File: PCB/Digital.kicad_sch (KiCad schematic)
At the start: 29 parts, among them IC1 MAX3051ESA+, J1 DE9_Pins_MountingHoles, J2 ICSP, J3 DE9_Plug_MountingHoles, J4 Conn_Coaxial, J6 Conn_01x03, J7 DOOR, J8 WINDOW, U1 PIC18F2580T-I/SO, Y2 ABLS

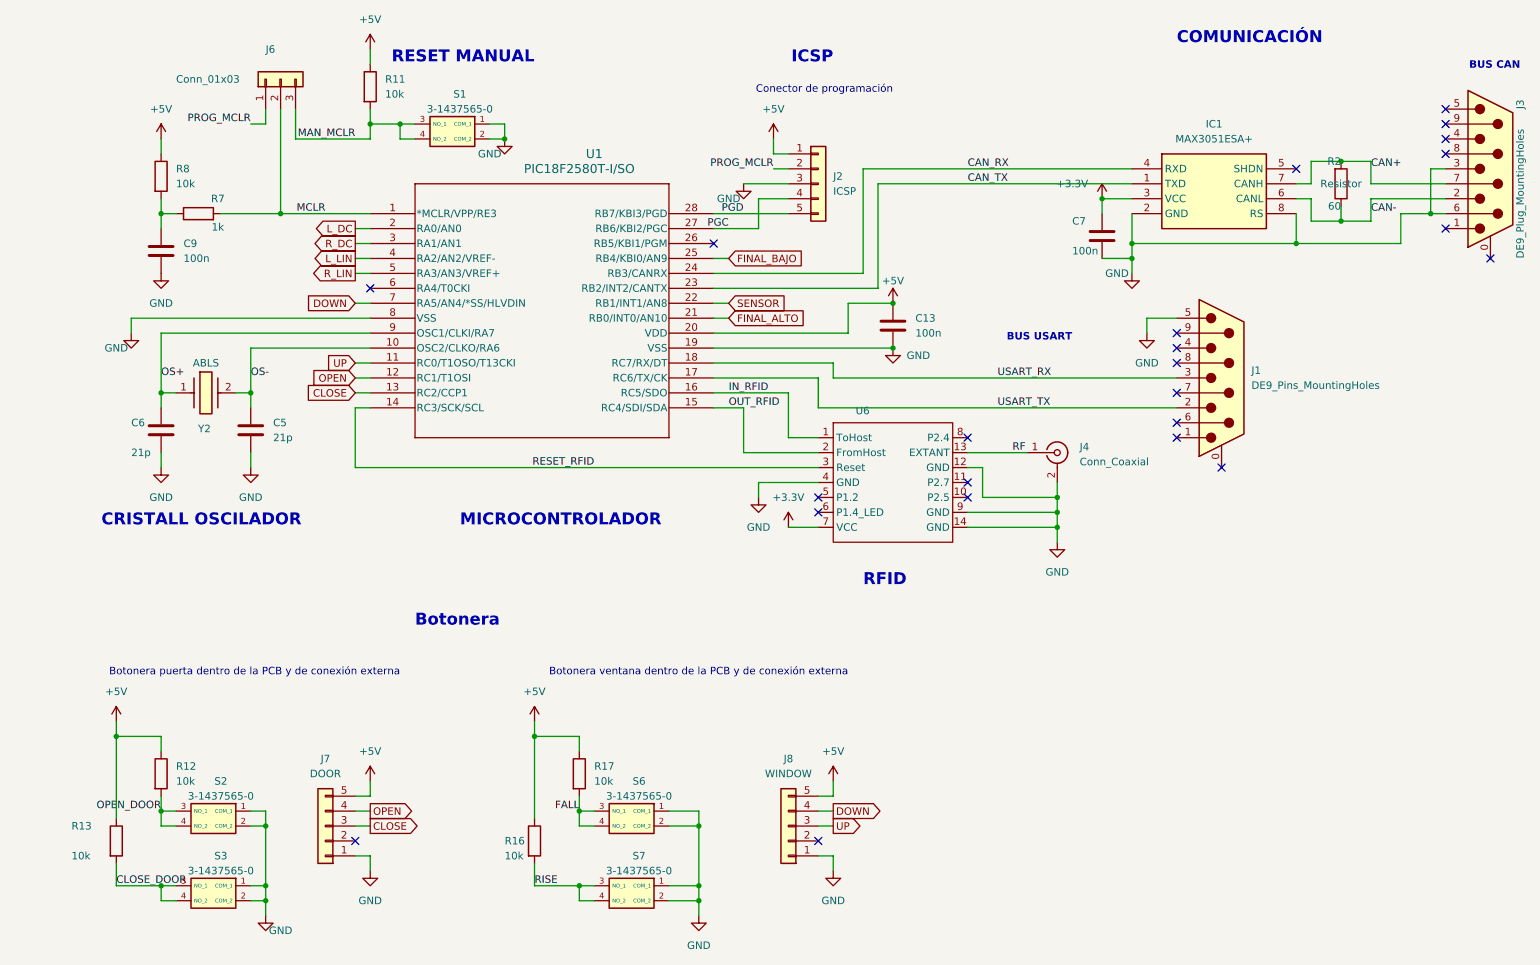
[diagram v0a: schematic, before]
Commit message: cambio de posición de los pines
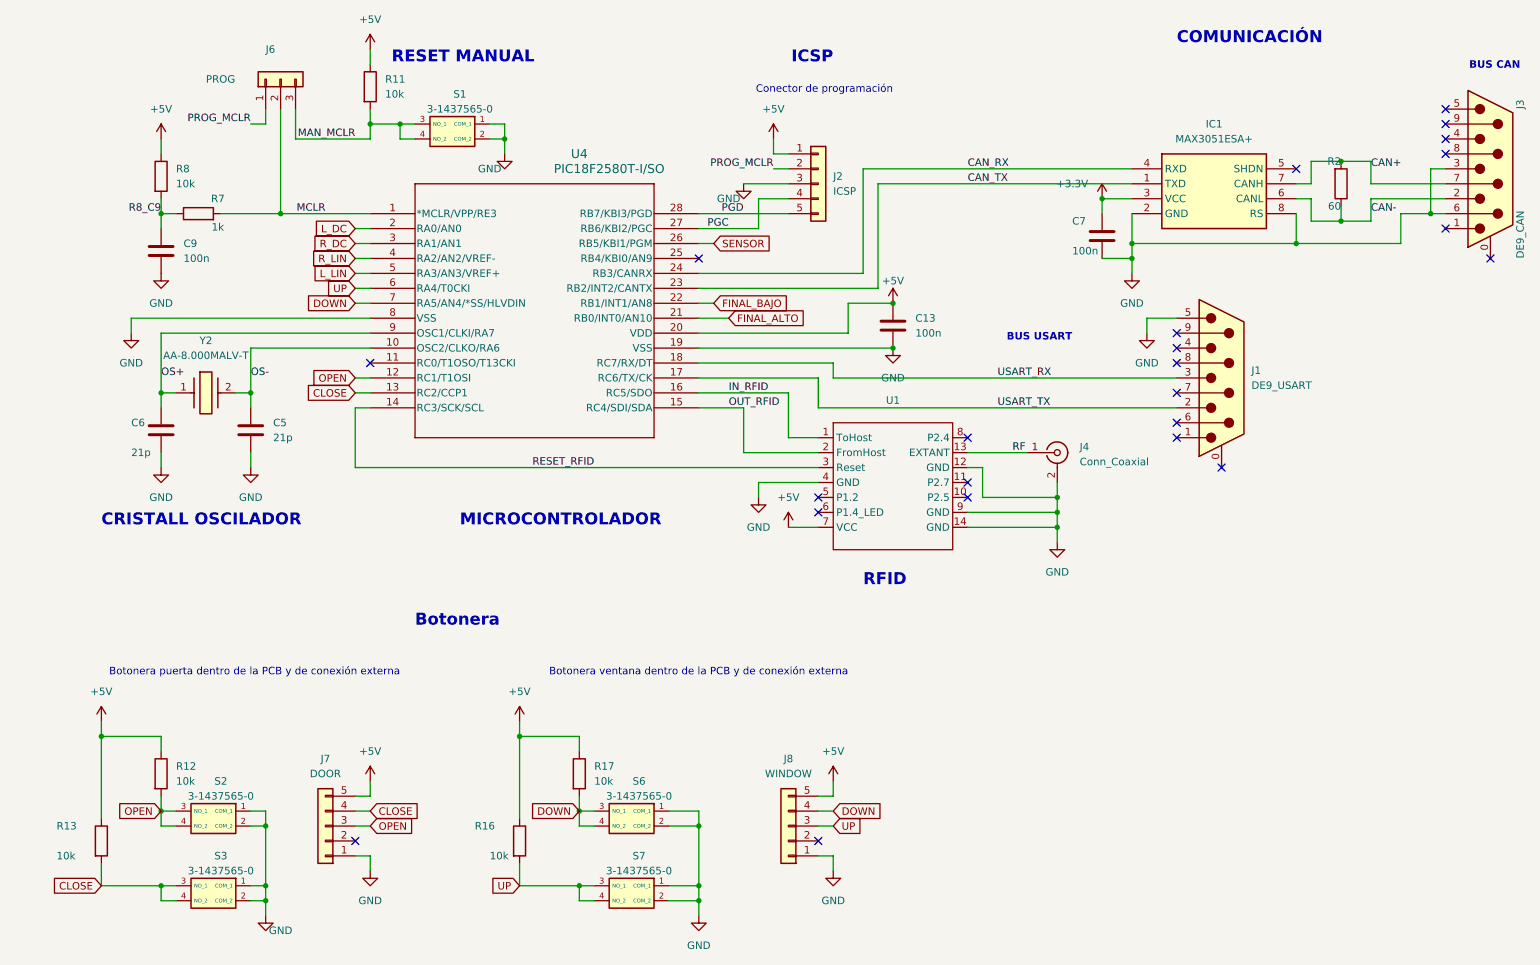
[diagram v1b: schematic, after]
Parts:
- removed U1: PIC18F2580T-I/SO, PIC18F2580T_I_SO:SOIC28-W_MC_MCH, symbol PIC18F2580T_I_SO:PIC18F2580T-I_SO
- removed U6: ~, CREATED:DLP-RFID2, symbol DLP-RFID2:DLP-RFID2
- removed Y2: ABLS, ABLS8000MHZB2T:ABLS8000MHZB2T, symbol ABLS-8_000MHZ-B2-T:ABLS-8.000MHZ-B2-T
- added U1: ~, DLP-RFID2:DLP-RFID2, symbol DLP-RFID2:DLP-RFID2
- added U4: PIC18F2580T-I/SO, PIC18F2580T_I_SO:SOIC28-W_MC_MCH, symbol PIC18F2580T_I_SO:PIC18F2580T-I_SO
- added Y2: AA-8.000MALV-T, AA-8.000MALV-T:AA8000MALVT, symbol AA-8.000MALV-T:AA-8.000MALV-T
- C5, C6: footprint Capacitor_SMD:C_0201_0603Metric -> Capacitor_SMD:C_0504_1310Metric
- J1: value DE9_Pins_MountingHoles -> DE9_USART
- J3: value DE9_Plug_MountingHoles -> DE9_CAN
- J6: value Conn_01x03 -> PROG
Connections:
- net CLOSE_DOOR is gone; now on net CLOSE: R13.2, S3.3 (NO_1), S3.4 (NO_2)
- net FALL is gone; now on net DOWN: R17.2, S6.3 (NO_1), S6.4 (NO_2)
- net OPEN_DOOR is gone; now on net OPEN: R12.2, S2.3 (NO_1), S2.4 (NO_2)
- net RISE is gone; now on net UP: R16.2, S7.3 (NO_1), S7.4 (NO_2)
- net +5V: now also U1.7 (VCC), U4.20 (VDD)
- net CAN_RX: now also U4.24 (RB3/CANRX)
- net CAN_TX: now also U4.23 (RB2/INT2/CANTX)
- net CLOSE: now also J7.4 (Pin_4), U4.13 (RC2/CCP1); no longer J7.3 (Pin_3)
- net DOWN: now also U4.7 (RA5/AN4/*SS/HLVDIN)
- net FINAL_ALTO: now also U4.21 (RB0/INT0/AN10)
- net FINAL_BAJO: now also U4.22 (RB1/INT1/AN8)
- net GND: now also U1.12 (GND), U1.14 (GND), U1.4 (GND), U1.9 (GND), U4.19 (VSS), U4.8 (VSS)
- net IN_RFID: now also U1.1 (ToHost), U4.16 (RC5/SDO)
- net L_DC: now also U4.2 (RA0/AN0)
- net L_LIN: now also U4.5 (RA3/AN3/VREF+)
- net MCLR: now also U4.1 (*MCLR/VPP/RE3)
- net OPEN: now also J7.3 (Pin_3), U4.12 (RC1/T1OSI); no longer J7.4 (Pin_4)
- net OS+: now also U4.9 (OSC1/CLKI/RA7), Y2.1
- net OS-: now also U4.10 (OSC2/CLKO/RA6), Y2.2
- net OUT_RFID: now also U1.2 (FromHost), U4.15 (RC4/SDI/SDA)
- net PGC: now also U4.27 (RB6/KBI2/PGC)
- net PGD: now also U4.28 (RB7/KBI3/PGD)
- net RESET_RFID: now also U1.3 (Reset), U4.14 (RC3/SCK/SCL)
- net RF: now also U1.13 (EXTANT)
- net R_DC: now also U4.3 (RA1/AN1)
- net R_LIN: now also U4.4 (RA2/AN2/VREF-)
- net SENSOR: now also U4.26 (RB5/KBI1/PGM)
- net UP: now also U4.6 (RA4/T0CKI)
- net USART_RX: now also U4.18 (RC7/RX/DT)
- net USART_TX: now also U4.17 (RC6/TX/CK)
- net R8_C9: now reaches C9.1, R7.1, R8.2
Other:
- moved on the sheet: R13, R16

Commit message: Update PCB
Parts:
- U1: value ~ -> DLP-RFID2
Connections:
- net MAN_MCLR: now also J6.2 (Pin_2); no longer J6.3 (Pin_3)
- net MCLR: now also J6.3 (Pin_3); no longer J6.2 (Pin_2)
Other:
- title: (none) -> Circuito digital
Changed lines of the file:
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@@
 	(generator_version "9.0")
 	(paper "A4")
+	(title_block
+		(title "Circuito digital")
+		(rev "4/4")
+	)
 	(text "CRISTALL OSCILADOR"
 		(exclude_from_sim no)
@@
 	)
 	(junction
-		(at 170.18 81.28)
+		(at 246.38 67.31)
 		(diameter 0)
 		(color 0 0 0 0)
 	)
 	(junction
-		(at 246.38 67.31)
+		(at 68.58 66.04)
 		(diameter 0)
 		(color 0 0 0 0)
@@
 	)
 	(junction
+		(at 170.18 81.28)
+		(diameter 0)
+		(color 0 0 0 0)
+	)
+	(junction
 		(at 35.56 154.94)
 		(diameter 0)
@@
 	)
 	(junction
-		(at 66.04 66.04)
-		(diameter 0)
-		(color 0 0 0 0)
-	)
-	(junction
 		(at 246.38 57.15)
 		(diameter 0)
@@
 	(wire
 		(pts
-			(xy 48.26 180.34) (xy 45.72 180.34)
+			(xy 68.58 48.26) (xy 68.58 66.04)
 		)
 		(stroke
@@
 	(wire
 		(pts
-			(xy 149.86 55.88) (xy 149.86 53.34)
+			(xy 48.26 180.34) (xy 45.72 180.34)
 		)
 		(stroke
@@
 	(wire
 		(pts
-			(xy 78.74 81.28) (xy 81.28 81.28)
+			(xy 149.86 55.88) (xy 149.86 53.34)
 		)
 		(stroke
@@
 	(wire
 		(pts
-			(xy 137.16 71.12) (xy 139.7 71.12)
+			(xy 78.74 81.28) (xy 81.28 81.28)
 		)
 		(stroke
@@
 	(wire
 		(pts
-			(xy 185.42 114.3) (xy 198.12 114.3)
+			(xy 137.16 71.12) (xy 139.7 71.12)
 		)
 		(stroke
@@
 	(wire
 		(pts
-			(xy 40.64 83.82) (xy 40.64 86.36)
+			(xy 185.42 114.3) (xy 198.12 114.3)
 		)
 		(stroke
@@
 	(wire
 		(pts
-			(xy 132.08 167.64) (xy 137.16 167.64)
+			(xy 40.64 83.82) (xy 40.64 86.36)
 		)
 		(stroke
@@
 	(wire
 		(pts
-			(xy 63.5 48.26) (xy 63.5 50.8)
+			(xy 132.08 167.64) (xy 137.16 167.64)
 		)
 		(stroke
@@
 	(wire
 		(pts
-			(xy 68.58 53.34) (xy 81.28 53.34)
-		)
-		(stroke
-			(width 0)
-			(type default)
-		)
-	)
-	(wire
-		(pts
 			(xy 86.36 50.8) (xy 88.9 50.8)
 		)
@@
 	(wire
 		(pts
-			(xy 66.04 66.04) (xy 81.28 66.04)
+			(xy 210.82 63.5) (xy 205.74 63.5)
 		)
 		(stroke
@@
 	(wire
 		(pts
-			(xy 210.82 63.5) (xy 205.74 63.5)
+			(xy 81.28 53.34) (xy 81.28 50.8)
 		)
 		(stroke
@@
 	(wire
 		(pts
-			(xy 81.28 53.34) (xy 81.28 50.8)
+			(xy 66.04 48.26) (xy 66.04 53.34)
 		)
 		(stroke
@@
 	(wire
 		(pts
+			(xy 68.58 66.04) (xy 81.28 66.04)
+		)
+		(stroke
+			(width 0)
+			(type default)
+		)
+	)
+	(wire
+		(pts
 			(xy 157.48 167.64) (xy 160.02 167.64)
 		)
@@
 	(wire
 		(pts
-			(xy 66.04 48.26) (xy 66.04 66.04)
-		)
-		(stroke
-			(width 0)
-			(type default)
-		)
-	)
-	(wire
-		(pts
 			(xy 132.08 180.34) (xy 137.16 180.34)
 		)
@@
 	(wire
 		(pts
-			(xy 68.58 48.26) (xy 68.58 53.34)
-		)
-		(stroke
-			(width 0)
-			(type default)
-		)
-	)
-	(wire
-		(pts
 			(xy 251.46 57.15) (xy 251.46 60.96)
 		)
@@
 	(wire
 		(pts
+			(xy 63.5 48.26) (xy 63.5 50.8)
+		)
+		(stroke
+			(width 0)
+			(type default)
+		)
+	)
+	(wire
+		(pts
 			(xy 45.72 167.64) (xy 48.26 167.64)
 		)
@@
 	(wire
 		(pts
+			(xy 170.18 78.74) (xy 170.18 81.28)
+		)
+		(stroke
+			(width 0)
+			(type default)
+		)
+	)
+	(wire
+		(pts
 			(xy 137.16 180.34) (xy 137.16 182.88)
 		)
@@
 	(wire
 		(pts
-			(xy 55.88 66.04) (xy 66.04 66.04)
+			(xy 55.88 66.04) (xy 68.58 66.04)
 		)
 		(stroke
@@
 	(wire
 		(pts
+			(xy 66.04 53.34) (xy 81.28 53.34)
+		)
+		(stroke
+			(width 0)
+			(type default)
+		)
+	)
+	(wire
+		(pts
 			(xy 162.56 86.36) (xy 162.56 81.28)
 		)
@@
 		(on_board yes)
 		(dnp no)
-		(fields_autoplaced yes)
 		(property "Reference" "U1"
 			(at 170.18 97.79 0)
@@
 			)
 		)
-		(property "Value" "~"
+		(property "Value" "DLP-RFID2"
 			(at 170.18 100.33 0)
 			(effects
@@
 	)
 	(symbol
+		(lib_id "power:+5V")
+		(at 170.18 78.74 0)
+		(unit 1)
+		(exclude_from_sim no)
+		(in_bom yes)
+		(on_board yes)
+		(dnp no)
+		(fields_autoplaced yes)
+		(property "Reference" "#PWR067"
+			(at 170.18 82.55 0)
+			(effects
+				(font
+					(size 1.27 1.27)
+				)
+				(hide yes)
+			)
+		)
+		(property "Value" "+5V"
+			(at 170.18 73.66 0)
+			(effects
+				(font
+					(size 1.27 1.27)
+				)
+			)
+		)
+		(property "Footprint" ""
+			(at 170.18 78.74 0)
+			(effects
+				(font
+					(size 1.27 1.27)
+				)
+				(hide yes)
+			)
+		)
+		(property "Datasheet" ""
+			(at 170.18 78.74 0)
+			(effects
+				(font
+					(size 1.27 1.27)
+				)
+				(hide yes)
+			)
+		)
+		(property "Description" "Power symbol creates a global label with name \"+5V\""
+			(at 170.18 78.74 0)
+			(effects
+				(font
+					(size 1.27 1.27)
+				)
+				(hide yes)
+			)
+		)
+		(pin "1"
+		)
+		(instances
+			(project ""
+				(path "/c96004bd-c0fc-431c-a510-eb1e1a82944f/ddbb6980-9f13-42d8-9727-7a64df9bde6c"
+					(reference "#PWR067")
+					(unit 1)
+				)
+			)
+		)
+	)
+	(symbol
 		(lib_name "GND_5")
 		(lib_id "power:GND")
@@
 					(unit 1)
 				)
-			)
-		)
-	)
-	(symbol
-		(lib_id "power:+5V")
-		(at 170.18 81.28 0)
-		(unit 1)
-		(exclude_from_sim no)
-		(in_bom yes)
-		(on_board yes)
-		(dnp no)
-		(property "Reference" "#PWR0102"
-			(at 170.18 85.09 0)
-			(effects
-				(font
-					(size 1.27 1.27)
-				)
-				(hide yes)
-			)
-		)
-		(property "Value" "+5V"
-			(at 170.18 77.47 0)
-			(effects
-				(font
-					(size 1.27 1.27)
-				)
-			)
-		)
-		(property "Footprint" ""
-			(at 170.18 81.28 0)
-			(effects
-				(font
-					(size 1.27 1.27)
-				)
-				(hide yes)
-			)
-		)
-		(property "Datasheet" ""
-			(at 170.18 81.28 0)
-			(effects
-				(font
-					(size 1.27 1.27)
-				)
-				(hide yes)
-			)
-		)
-		(property "Description" ""
-			(at 170.18 81.28 0)
-			(effects
-				(font
-					(size 1.27 1.27)
-				)
-			)
-		)
-		(pin "1"
-		)
-		(instances
-			(project "puertas"
-				(path "/c96004bd-c0fc-431c-a510-eb1e1a82944f/ddbb6980-9f13-42d8-9727-7a64df9bde6c"
-					(reference "#PWR0102")
-					(unit 1)
-				)
-			)
-			(project "Digital"
-				(path "/fabbde56-8e14-4a1d-9ecb-2c0209abd5e9"
-					(reference "#PWR01")
-					(unit 1)
-				)
